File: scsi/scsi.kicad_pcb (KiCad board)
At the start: 2 copper layers, 100 x 90 mm, 13 parts, among them J1 SCSI, J2 VAMPIRE_OR_HBA, J3 ENABLE_TERMINATION, J4 CPU, U1 AM33C93

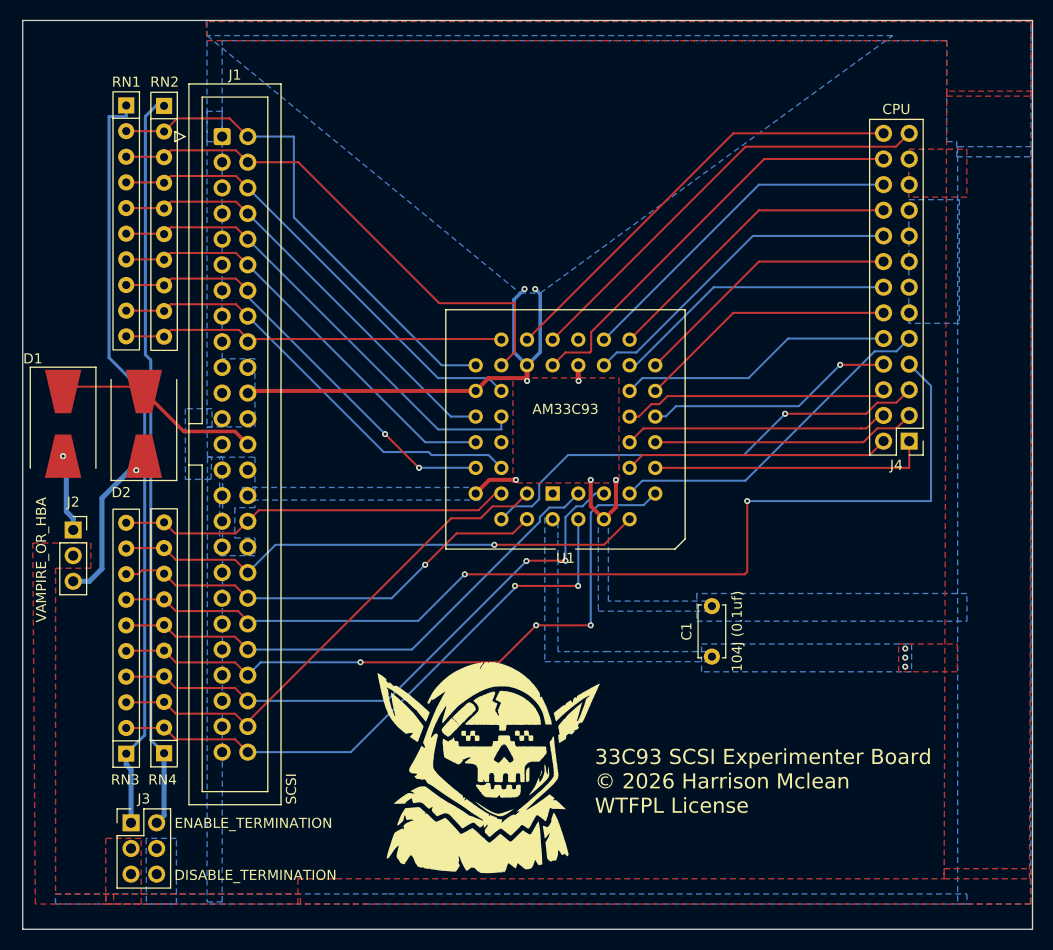
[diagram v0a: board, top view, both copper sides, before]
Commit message: Fancied up board graphics
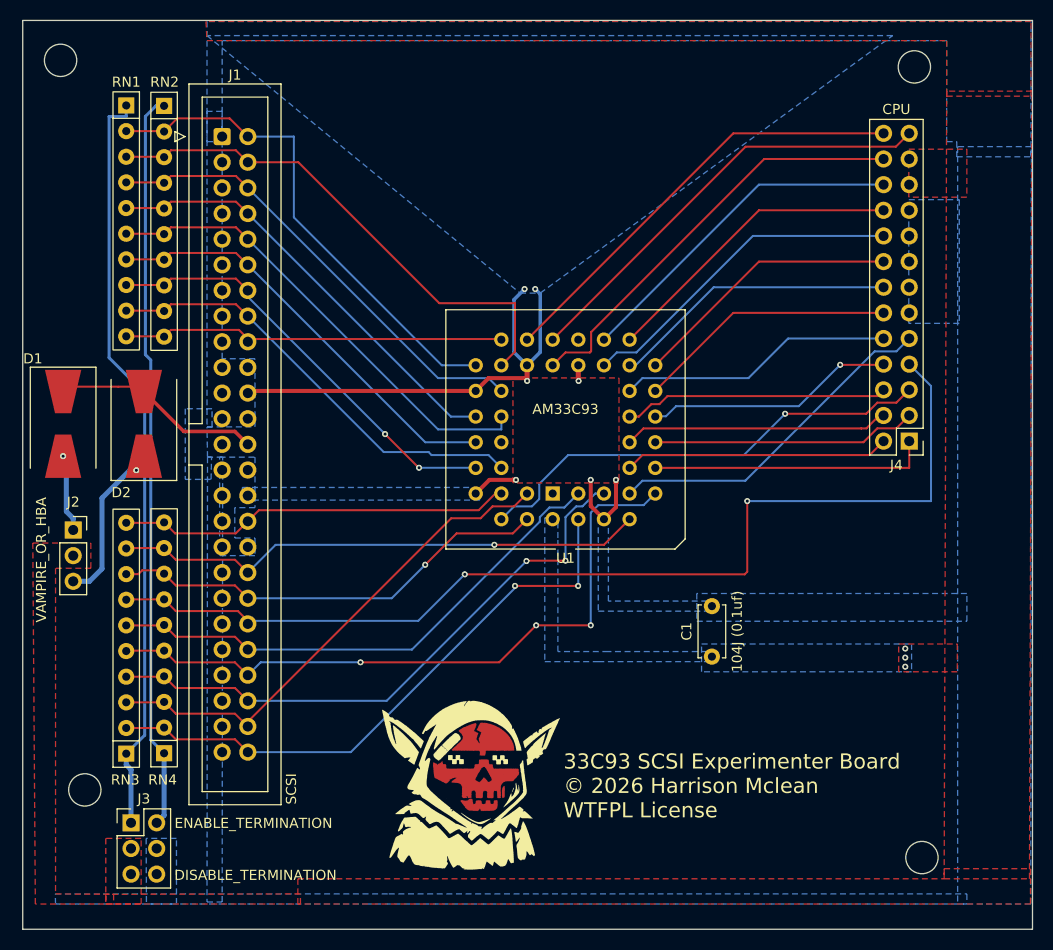
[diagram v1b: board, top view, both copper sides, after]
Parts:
- removed the G*** at (72.4, 103.5)
- added ?: , , F.Cu at (32.4, 105.7)
- added ?: , , F.Cu at (114.5, 34.1)
- added ?: , , F.Cu at (115.3, 112.4)
- added G*** (x2): LOGO, LOGO, F.Cu at (71.1, 103.4)
- added G***: LOGO, LOGO, F.Cu at (70.7, 105.2)
- added REF**: MountingHole_3.2mm_M3, MountingHole:MountingHole_3.2mm_M3, F.Cu at (30.0, 33.5)
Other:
- board text added: "REF**"

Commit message: Fixed mounting holes
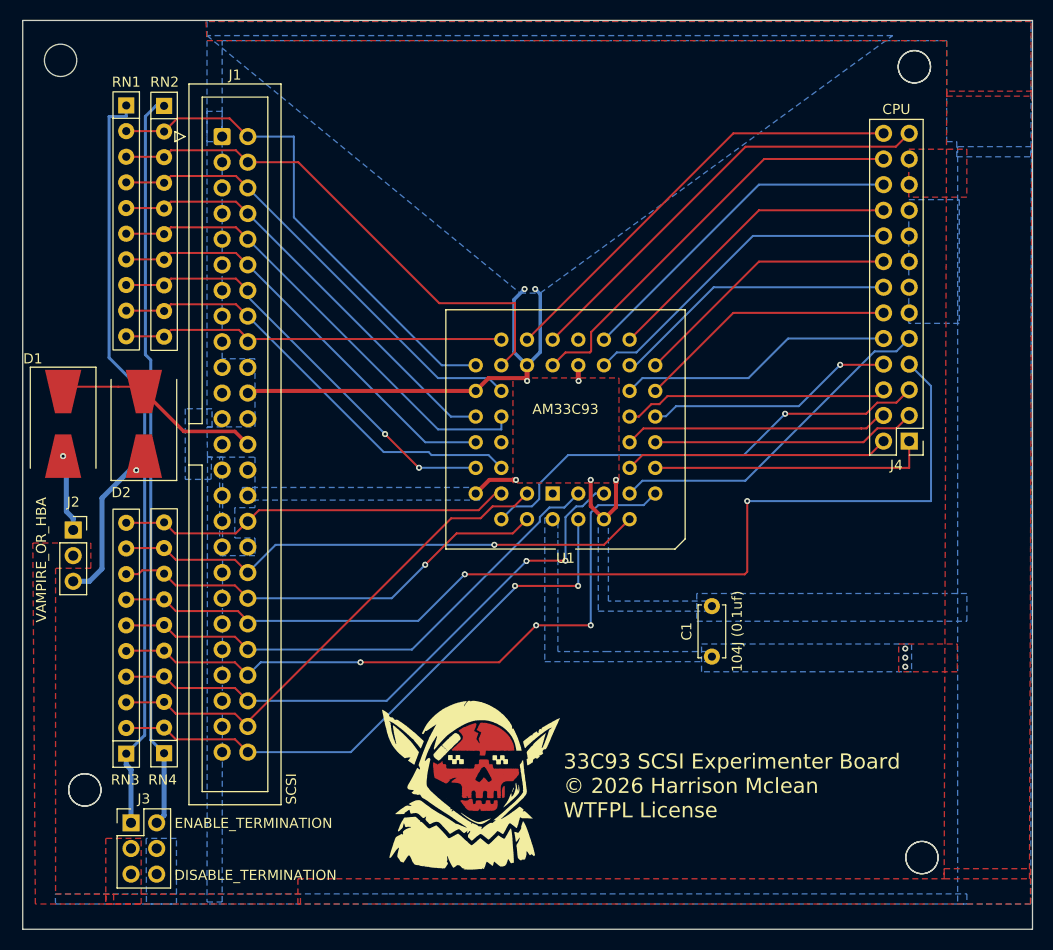
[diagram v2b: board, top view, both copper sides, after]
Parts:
- added REF**: MountingHole_3.2mm_M3, MountingHole:MountingHole_3.2mm_M3, F.Cu at (114.5, 34.1)
- added REF**: MountingHole_3.2mm_M3, MountingHole:MountingHole_3.2mm_M3, F.Cu at (32.4, 105.7)
- added REF**: MountingHole_3.2mm_M3, MountingHole:MountingHole_3.2mm_M3, F.Cu at (115.3, 112.4)
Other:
- board text removed: "REF**"
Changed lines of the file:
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@@
 		)
 	)
+	(footprint "MountingHole:MountingHole_3.2mm_M3"
+		(layer "F.Cu")
+		(at 114.55 34.075)
+		(descr "Mounting Hole 3.2mm, M3, no annular, generated by kicad-footprint-generator mountinghole.py")
+		(tags "mountinghole M3")
+		(property "Reference" "REF**"
+			(at 0 -4.15 0)
+			(layer "F.SilkS")
+			(hide yes)
+			(effects
+				(font
+					(size 1 1)
+					(thickness 0.15)
+				)
+			)
+		)
+		(property "Value" "MountingHole_3.2mm_M3"
+			(at 0 4.15 0)
+			(layer "F.Fab")
+			(hide yes)
+			(effects
+				(font
+					(size 1 1)
+					(thickness 0.15)
+				)
+			)
+		)
+		(property "Datasheet" ""
+			(at 0 0 0)
+			(layer "F.Fab")
+			(hide yes)
+			(effects
+				(font
+					(size 1.27 1.27)
+					(thickness 0.15)
+				)
+			)
+		)
+		(property "Description" ""
+			(at 0 0 0)
+			(layer "F.Fab")
+			(hide yes)
+			(effects
+				(font
+					(size 1.27 1.27)
+					(thickness 0.15)
+				)
+			)
+		)
+		(attr exclude_from_pos_files exclude_from_bom)
+		(fp_circle
+			(center 0 0)
+			(end 3.2 0)
+			(stroke
+				(width 0.15)
+				(type solid)
+			)
+			(fill no)
+			(layer "Cmts.User")
+		)
+		(fp_circle
+			(center 0 0)
+			(end 3.45 0)
+			(stroke
+				(width 0.05)
+				(type solid)
+			)
+			(fill no)
+			(layer "F.CrtYd")
+		)
+		(pad "" np_thru_hole circle
+			(at 0 0)
+			(size 3.2 3.2)
+			(drill 3.2)
+			(layers "*.Cu" "*.Mask")
+		)
+		(embedded_fonts no)
+	)
 	(footprint "Connector_PinSocket_2.54mm:PinSocket_1x03_P2.54mm_Vertical"
 		(layer "F.Cu")
@@
 			(at 0 4.15 0)
 			(layer "F.Fab")
+			(hide yes)
 			(effects
 				(font
@@
 			(layer "F.CrtYd")
 		)
-		(fp_text user "${REFERENCE}"
-			(at 0 0 0)
-			(layer "F.Fab")
-			(effects
-				(font
-					(size 1 1)
-					(thickness 0.15)
-				)
-			)
-		)
 		(pad "" np_thru_hole circle
 			(at 0 0)
@@
 		)
 	)
+	(footprint "MountingHole:MountingHole_3.2mm_M3"
+		(layer "F.Cu")
+		(at 32.4 105.7)
+		(descr "Mounting Hole 3.2mm, M3, no annular, generated by kicad-footprint-generator mountinghole.py")
+		(tags "mountinghole M3")
+		(property "Reference" "REF**"
+			(at 0 -4.15 0)
+			(layer "F.SilkS")
+			(hide yes)
+			(effects
+				(font
+					(size 1 1)
+					(thickness 0.15)
+				)
+			)
+		)
+		(property "Value" "MountingHole_3.2mm_M3"
+			(at 0 4.15 0)
+			(layer "F.Fab")
+			(hide yes)
+			(effects
+				(font
+					(size 1 1)
+					(thickness 0.15)
+				)
+			)
+		)
+		(property "Datasheet" ""
+			(at 0 0 0)
+			(layer "F.Fab")
+			(hide yes)
+			(effects
+				(font
+					(size 1.27 1.27)
+					(thickness 0.15)
+				)
+			)
+		)
+		(property "Description" ""
+			(at 0 0 0)
+			(layer "F.Fab")
+			(hide yes)
+			(effects
+				(font
+					(size 1.27 1.27)
+					(thickness 0.15)
+				)
+			)
+		)
+		(attr exclude_from_pos_files exclude_from_bom)
+		(fp_circle
+			(center 0 0)
+			(end 3.2 0)
+			(stroke
+				(width 0.15)
+				(type solid)
+			)
+			(fill no)
+			(layer "Cmts.User")
+		)
+		(fp_circle
+			(center 0 0)
+			(end 3.45 0)
+			(stroke
+				(width 0.05)
+				(type solid)
+			)
+			(fill no)
+			(layer "F.CrtYd")
+		)
+		(pad "" np_thru_hole circle
+			(at 0 0)
+			(size 3.2 3.2)
+			(drill 3.2)
+			(layers "*.Cu" "*.Mask")
+		)
+		(embedded_fonts no)
+	)
 	(footprint "LOGO"
 		(layer "F.Cu")
@@
 		(embedded_fonts no)
 	)
+	(footprint "MountingHole:MountingHole_3.2mm_M3"
+		(layer "F.Cu")
+		(at 115.3 112.4)
+		(descr "Mounting Hole 3.2mm, M3, no annular, generated by kicad-footprint-generator mountinghole.py")
+		(tags "mountinghole M3")
+		(property "Reference" "REF**"
+			(at 0 -4.15 0)
+			(layer "F.SilkS")
+			(hide yes)
+			(effects
+				(font
+					(size 1 1)
+					(thickness 0.15)
+				)
+			)
+		)
+		(property "Value" "MountingHole_3.2mm_M3"
+			(at 0 4.15 0)
+			(layer "F.Fab")
+			(hide yes)
+			(effects
+				(font
+					(size 1 1)
+					(thickness 0.15)
+				)
+			)
+		)
+		(property "Datasheet" ""
+			(at 0 0 0)
+			(layer "F.Fab")
+			(hide yes)
+			(effects
+				(font
+					(size 1.27 1.27)
+					(thickness 0.15)
+				)
+			)
+		)
+		(property "Description" ""
+			(at 0 0 0)
+			(layer "F.Fab")
+			(hide yes)
+			(effects
+				(font
+					(size 1.27 1.27)
+					(thickness 0.15)
+				)
+			)
+		)
+		(attr exclude_from_pos_files exclude_from_bom)
+		(fp_circle
+			(center 0 0)
+			(end 3.2 0)
+			(stroke
+				(width 0.15)
+				(type solid)
+			)
+			(fill no)
+			(layer "Cmts.User")
+		)
+		(fp_circle
+			(center 0 0)
+			(end 3.45 0)
+			(stroke
+				(width 0.05)
+				(type solid)
+			)
+			(fill no)
+			(layer "F.CrtYd")
+		)
+		(pad "" np_thru_hole circle
+			(at 0 0)
+			(size 3.2 3.2)
+			(drill 3.2)
+			(layers "*.Cu" "*.Mask")
+		)
+		(embedded_fonts no)
+	)
 	(footprint "Resistor_THT:R_Array_SIP10"
 		(layer "F.Cu")
@@
 		)
 	)
-	(gr_text "REF**"
-		(at 115.3 112.4 0)
-		(layer "F.Fab")
-		(effects
-			(font
-				(size 1 1)
-				(thickness 0.15)
-			)
-		)
-	)
-	(gr_text "REF**"
-		(at 114.55 34.1 0)
-		(layer "F.Fab")
-		(effects
-			(font
-				(size 1 1)
-				(thickness 0.15)
-			)
-		)
-	)
-	(gr_text "REF**"
-		(at 32.4 105.7 0)
-		(layer "F.Fab")
-		(effects
-			(font
-				(size 1 1)
-				(thickness 0.15)
-			)
-		)
-	)
